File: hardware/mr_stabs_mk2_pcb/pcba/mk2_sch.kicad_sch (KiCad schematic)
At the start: 69 parts, among them U1 INA228, U2 TPS54202DDC, U3 AP2112K-3.3, U4 BNO055, U5 USBLC6-2SC6, Y1 32.768kHz

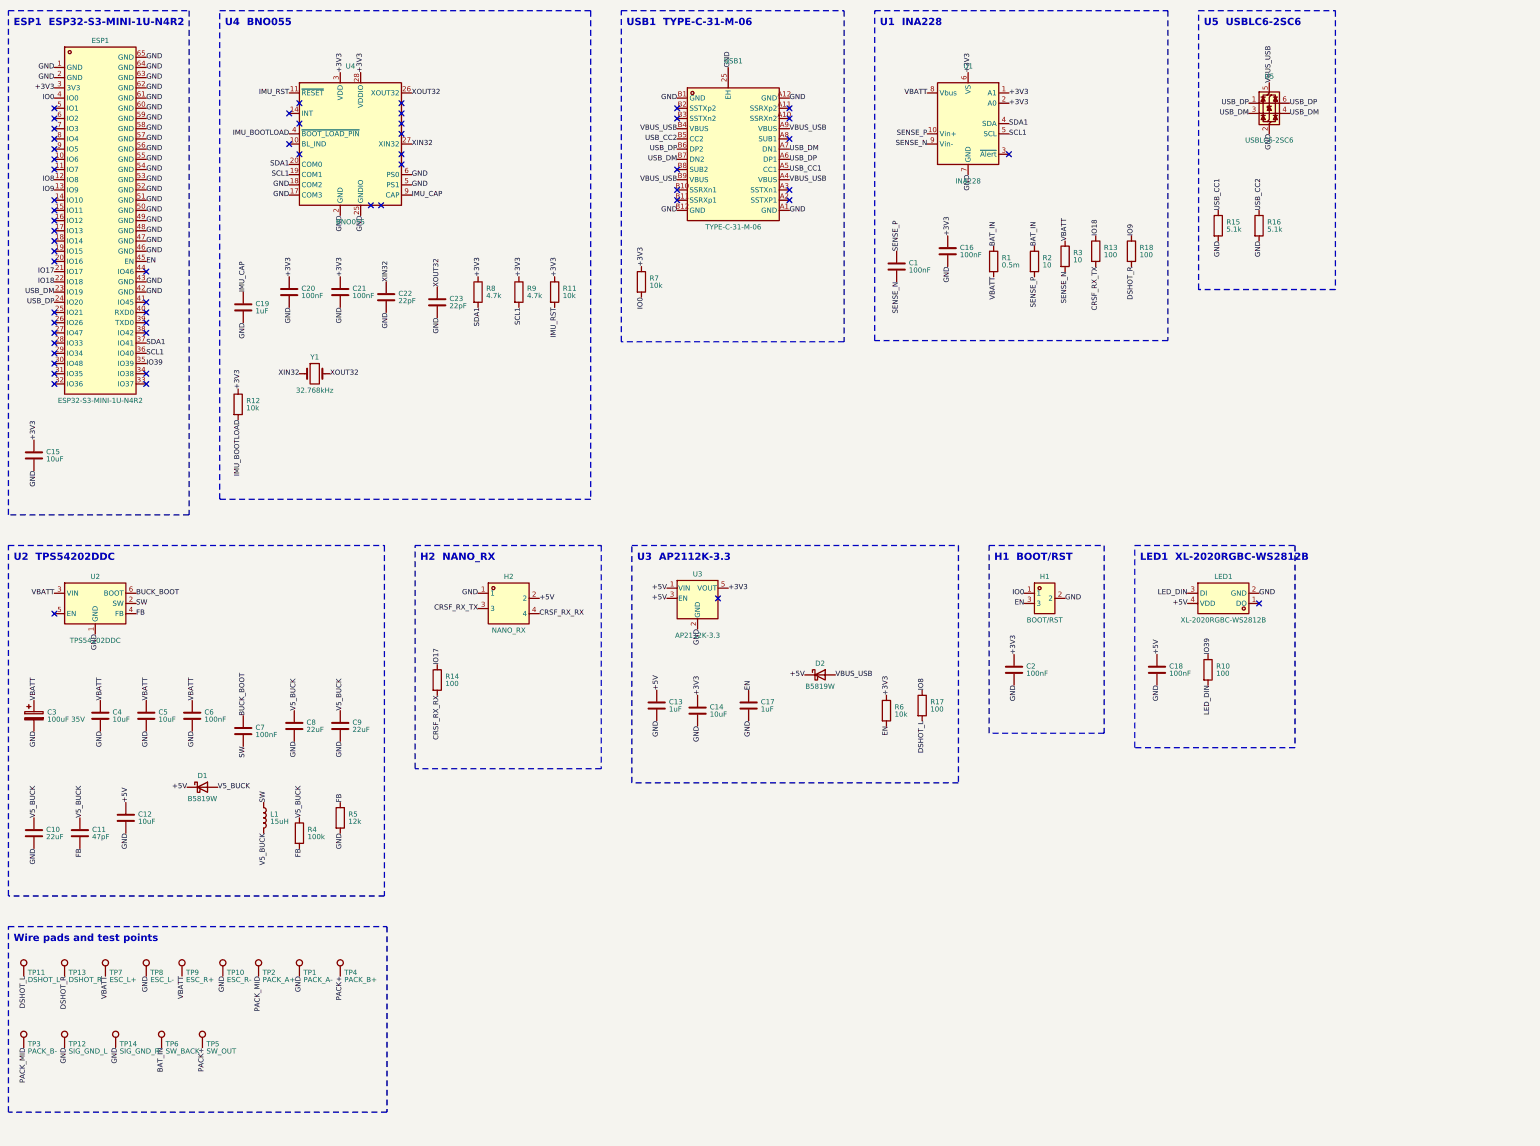
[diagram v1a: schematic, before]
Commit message: Stand the Nano RX on a right-angle header and align the STEP models
- H2 is now an HX PZ2.54-1x4P WT right-angle SMD header (C46061677) at the stem's rear, pins
  pointing forward; the RX slides on and stands 18 mm toward the wedge. A vertical header would
  have laid it flat. Rotated 180 deg because KiCad mirrors bottom-side footprints and
  legalize.py does not; at 0 deg its pins pointed out past the rear edge.
- EasyEDA's footprints now use their STEP models, offset to match the VRML the renders use
  (align_models.py): the USB-C's STEP sat 2.55 mm low and the headers' 2.5 to 3.8 mm along the
  row, so the exported STEP disagreed with the render.
- New build123d model of the right-angle header; datasheet review for H2.
- Re-routed: 0 errors, 0 unconnected. Order files, STEP and simulations regenerated.

Co-Authored-By: Claude Opus 5.5 <noreply@anthropic.com>
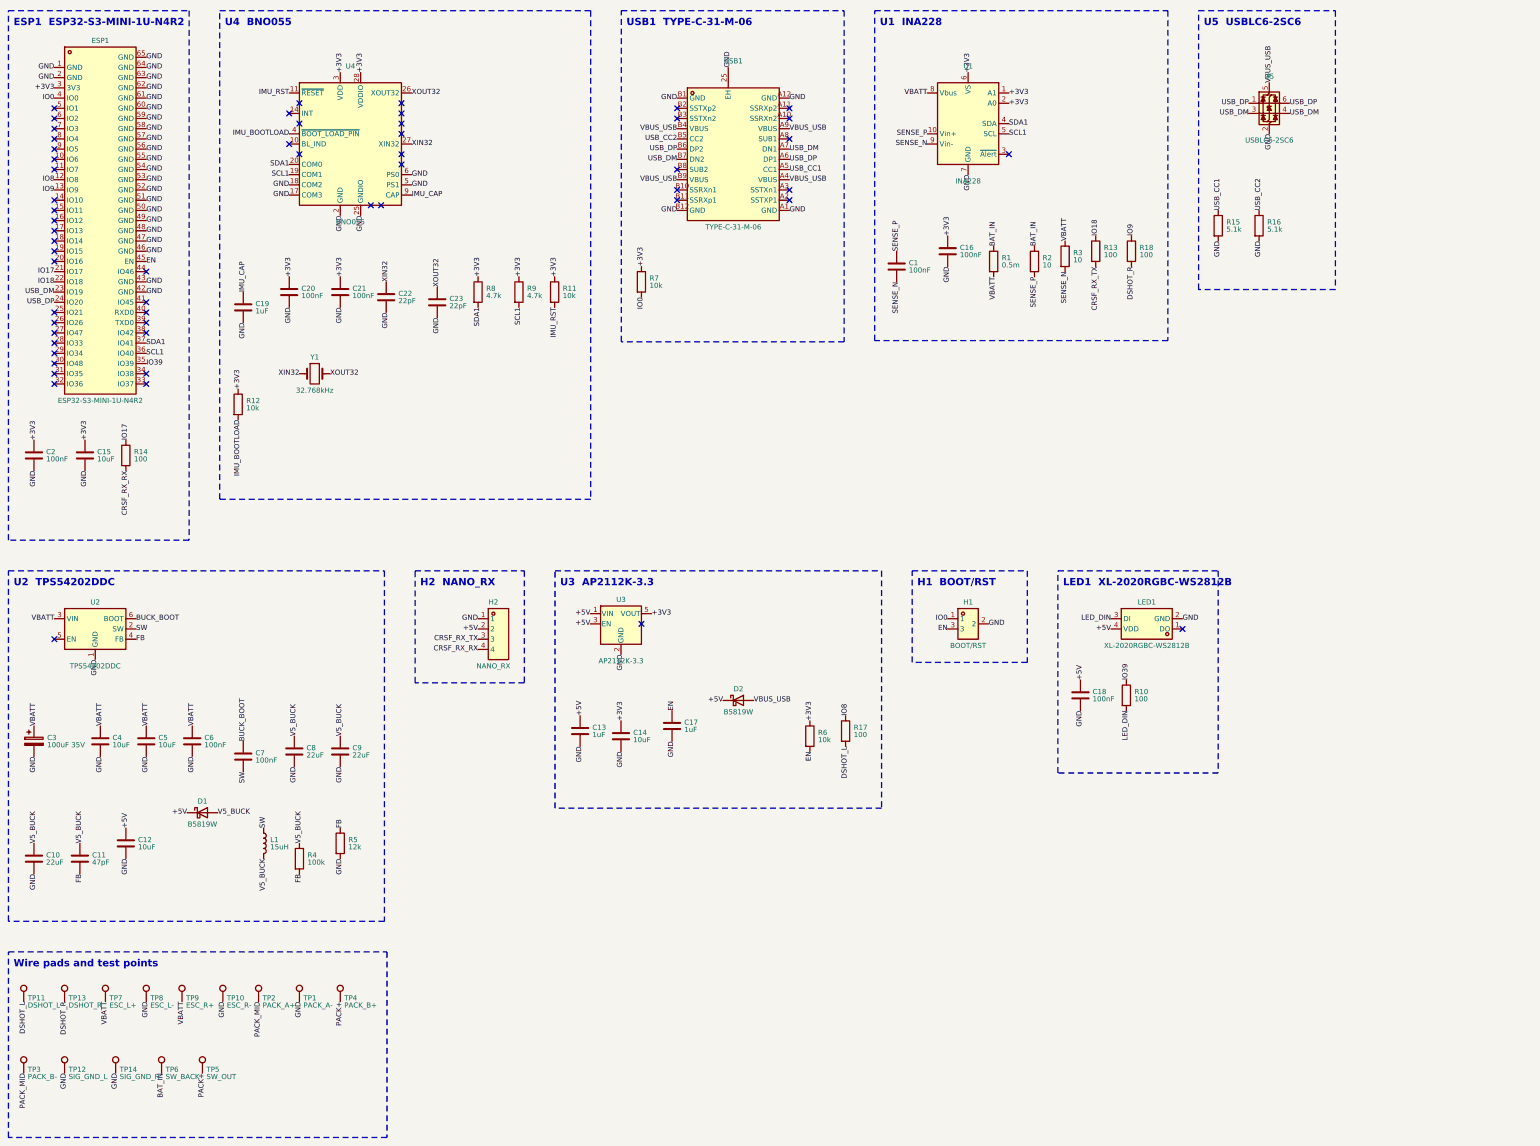
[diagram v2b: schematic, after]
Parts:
- removed C1, C16, C2, C20: 100nF, symbol Device:C
- removed C13, C19: 1uF, symbol Device:C
- removed C3: 100uF 35V, symbol Device:C_Polarized
- removed C4: 10uF, symbol Device:C
- removed R15: 5.1k, symbol Device:R
- added H1: BOOT/RST, symbol mk2:HXPZ2.54-1X3PTP-YQ
- added H2: NANO_RX, symbol mk2:HXPZ2.54-1X4PWT
- added R18: 100, symbol Device:R
- added R5: 12k, symbol Device:R
- added U2: TPS54202DDC, symbol Regulator_Switching:TPS54202DDC
- added U4: BNO055, symbol Sensor_Motion:BNO055
- added U5: USBLC6-2SC6, symbol Power_Protection:USBLC6-2SC6
- added USB1: TYPE-C-31-M-06, symbol mk2:TYPE-C-31-M-06
- added Y1: 32.768kHz, symbol Device:Crystal
- C1: renamed from R1; value 0.5m -> 100nF; symbol Device:R -> Device:C
- C10: renamed from C12; value 10uF -> 22uF
- C11: renamed from D1; value B5819W -> 47pF; symbol Device:D_Schottky -> Device:C
- C12: renamed from L1; value 15uH -> 10uF; symbol Device:L -> Device:C
- C13: renamed from C14; value 10uF -> 1uF
- C14: renamed from C17; value 1uF -> 10uF
- C15: renamed from U4; value BNO055 -> 10uF; symbol Sensor_Motion:BNO055 -> Device:C
- C16: renamed from R2; value 10 -> 100nF; symbol Device:R -> Device:C
- C17: renamed from D2; value B5819W -> 1uF; symbol Device:D_Schottky -> Device:C
- C19: renamed from C21; value 100nF -> 1uF
- C2: renamed from C15; value 10uF -> 100nF
- C20: renamed from C22; value 22pF -> 100nF
- C21: renamed from C23; value 22pF -> 100nF
- C22: renamed from R8; value 4.7k -> 22pF; symbol Device:R -> Device:C
- C23: renamed from R9; value 4.7k -> 22pF; symbol Device:R -> Device:C
- C3: renamed from C5; value 10uF -> 100uF 35V; symbol Device:C -> Device:C_Polarized
- C4: renamed from C6; value 100nF -> 10uF
- C5: renamed from C7; value 100nF -> 10uF
- C6: renamed from C8; value 22uF -> 100nF
- C7: renamed from C9; value 22uF -> 100nF
- C9: renamed from C11; value 47pF -> 22uF
- D1: renamed from R4; value 100k -> B5819W; symbol Device:R -> Device:D_Schottky
- D2: renamed from R6; value 10k -> B5819W; symbol Device:R -> Device:D_Schottky
- L1: renamed from R5; value 12k -> 15uH; symbol Device:R -> Device:L
- R1: renamed from R3; value 10 -> 0.5m
- R11: renamed from Y1; value 32.768kHz -> 10k; symbol Device:Crystal -> Device:R
- R12: renamed from USB1; value TYPE-C-31-M-06 -> 10k; symbol mk2:TYPE-C-31-M-06 -> Device:R
- R13: renamed from U5; value USBLC6-2SC6 -> 100; symbol Power_Protection:USBLC6-2SC6 -> Device:R
- R15: renamed from U2; value TPS54202DDC -> 5.1k; symbol Regulator_Switching:TPS54202DDC -> Device:R
- R17: renamed from H1; value BOOT/RST -> 100; symbol mk2:HXPZ2.54-1X3PTP-YQ -> Device:R
- R2: renamed from R13; value 100 -> 10
- R3: renamed from R18; value 100 -> 10
- R4: renamed from H2; value NANO_RX -> 100k; symbol mk2:HXPZ2.54-1X4PTP-YQ -> Device:R
- R6: renamed from R17; value 100 -> 10k
- R8: renamed from R11; value 10k -> 4.7k
- R9: renamed from R12; value 10k -> 4.7k
- renumbered C10 to C8
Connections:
- net +3V3: now also C14.1, C15.1, C16.1, C20.1, C21.1, R11.1, R12.1, R6.1, U4.28 (VDDIO), U4.3 (VDD); no longer C13.1, C15.28 (VDDIO), C15.3 (VDD), C19.1, C22.1, C23.1, D2.1
- net +5V: now also C12.1, C13.1, D1.1 (K), D2.1 (K), H2.2; no longer C10.1, C11.1 (K), C17.1 (K), R4.2
- net BAT_IN: now also R1.1, R2.1; no longer C1.1, C16.1
- net BUCK_BOOT: now also C7.1, U2.6 (BOOT); no longer C5.1, R15.6 (BOOT)
- net CRSF_RX_RX: now also H2.4; no longer R4.4
- net CRSF_RX_TX: now also R13.2, H2.3; no longer R2.2, R4.3
- net DSHOT_L: now also R17.2; no longer R6.2
- net DSHOT_R: now also R18.2; no longer R3.2
- net EN: now also C17.1, R6.2, H1.3; no longer C14.1, D2.2, R17.3
- net FB: now also C11.2, R4.2, R5.1, U2.4 (FB); no longer C9.2, D1.2, L1.1, R15.4 (FB)
- net GND: now also C12.2, C16.2, C17.2, C22.2, C23.2, C5.2, C9.2, R15.2, H1.2, H2.1, R5.2, U2.1 (GND), U4.17 (COM3), U4.18 (COM2), U4.2 (GND), U4.25 (GNDIO), U4.5 (PS1), U4.6 (PS0), U5.2 (GND), USB1.25 (EH), USB1.A1 (GND), USB1.A12 (GND), USB1.B1 (GND), USB1.B12 (GND); no longer C15.17 (COM3), C15.18 (COM2), C15.25 (GNDIO), C15.5 (PS1), C15.6 (PS0), C7.2, L1.2, R12.25 (EH), R12.A1 (GND), R12.A12 (GND), R12.B1 (GND), R12.B12 (GND), R13.2 (GND), R15.1 (GND), R17.2, R4.1
- net IMU_BOOTLOAD: now also R12.2, U4.4 (~{BOOT_LOAD_PIN}); no longer C15.4 (~{BOOT_LOAD_PIN}), R9.2
- net IMU_CAP: now also C19.1, U4.9 (CAP); no longer C15.9 (CAP)
- net IMU_RST: now also R11.2, U4.11 (~{RESET}); no longer C15.11 (~{RESET}), R8.2
- net IO0: now also H1.1; no longer R17.1
- net IO18: now also R13.1; no longer R2.1
- net IO8: now also R17.1; no longer R6.1
- net IO9: now also R18.1; no longer R3.1
- net SCL1: now also R9.2, U4.19 (COM1); no longer C15.19 (COM1), C23.2
- net SDA1: now also R8.2, U4.20 (COM0); no longer C15.20 (COM0), C22.2
- net SENSE_N: now also C1.2, R3.2; no longer R1.2
- net SENSE_P: now also C1.1, R2.2; no longer C16.2
- net SW: now also C7.2, L1.1, U2.2 (SW); no longer C12.1, C5.2, R15.2 (SW)
- net USB_CC1: now also R15.1, USB1.A5 (CC1); no longer R12.A5 (CC1)
- net USB_CC2: now also USB1.B5 (CC2); no longer R12.B5 (CC2)
- net USB_DM: now also U5.3 (I/O2), U5.4 (I/O2), USB1.A7 (DN1), USB1.B7 (DN2); no longer R12.A7 (DN1), R12.B7 (DN2), R13.3 (I/O2), R13.4 (I/O2)
- net USB_DP: now also U5.1 (I/O1), U5.6 (I/O1), USB1.A6 (DP1), USB1.B6 (DP2); no longer R12.A6 (DP1), R12.B6 (DP2), R13.1 (I/O1), R13.6 (I/O1)
- net V5_BUCK: now also C10.1, C11.1, D1.2 (A), L1.2, R4.1; no longer C11.2 (A), C12.2, C6.1, C7.1, D1.1
- net VBATT: now also C5.1, C6.1, R1.2, R3.1, U2.3 (VIN); no longer C1.2, R1.1, R15.3 (VIN)
- net VBUS_USB: now also D2.2 (A), U5.5 (VBUS), USB1.A4 (VBUS), USB1.A9 (VBUS), USB1.B4 (VBUS), USB1.B9 (VBUS); no longer C17.2 (A), R12.A4 (VBUS), R12.A9 (VBUS), R12.B4 (VBUS), R12.B9 (VBUS), R13.5 (VBUS)
- net XIN32: now also C22.1, U4.27 (XIN32), Y1.1; no longer C15.27 (XIN32), C20.1, R11.1
- net XOUT32: now also C23.1, U4.26 (XOUT32), Y1.2; no longer C15.26 (XOUT32), C21.1, R11.2
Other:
- moved on the sheet: C10, C13, C14, C18, C19, C20, C21, C4, C5, C6, C7, C8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
